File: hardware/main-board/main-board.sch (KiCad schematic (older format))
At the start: 92 parts, among them J1 BARREL_JACK, J2 CONN_01X10, J3 CONN_01X10, J4 USB_OTG, J5 CONN_02X05, J6 SMA, Q1 DDTD113ZC, Q2 DDTD113ZC, Q3 DDTD113ZC, Q4 DDTD113ZC, Q5 DDTD113ZC, Q6 FDB14N30TM, Q7 DDTD113ZC, Q8 DDTD113ZC, Q9 DDTD113ZC, SW1 SW_Push, SW2 SW_Push, SW3 SW_Push, SW4 SW_Push, U1 LD1117S33TR, U2 MAX1771, U3 STM32F302C, U4 FGPMMOPA6H, Y1 8MHz, Y2 32.768kHz

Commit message: Working on main board schematic
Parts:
- C10, C8: footprint (none) -> Capacitors_SMD:C_0805; Part (none) -> 311-1365-1-ND; Source (none) -> DigiKey
- C12: footprint (none) -> Capacitors_SMD:C_0603; Part (none) -> 311-1085-1-ND; Source (none) -> DigiKey
- C13, C17: value C -> 16p; footprint (none) -> Capacitors_SMD:C_0603; Part (none) -> 311-1751-1-ND; Source (none) -> DigiKey
- C16: footprint Capacitors_SMD:C_0603 -> Capacitors_SMD:C_0805; Part (none) -> 311-1365-1-ND
- C18: Part (none) -> 311-1085-1-ND
- C19, C20: value C -> 5p; footprint (none) -> Capacitors_SMD:C_0603; Part (none) -> 311-1054-1-ND; Source (none) -> DigiKey
- C2: footprint (none) -> Capacitors_SMD:C_0805; Part (none) -> 311-1460-1-ND; Source (none) -> DigiKey
- C4: value CP -> 150u
- C5, C6: value CP -> 3.3u; footprint (none) -> Capacitors_ThroughHole:CP_Radial_D6.3mm_P2.50mm; Part (none) -> 493-12639-1-ND; Source (none) -> DigiKey
- J5: Part (none) -> NA; Source (none) -> NA
- TP1, TP2, TP3, TP4, TP5, TP6: Part (none) -> NA; Source DigiKey -> NA
- Y1: footprint (none) -> Crystals:Crystal_SMD_HC49-SD; Part (none) -> 535-10212-1-ND; Source (none) -> DigiKey
- Y2: footprint (none) -> radio-clock:ABS07; Part (none) -> 535-9542-1-ND; Source (none) -> DigiKey
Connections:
- wire segments 360 -> 291
- no-connect marks 5 -> 6
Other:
- moved on the sheet: BT1, C8

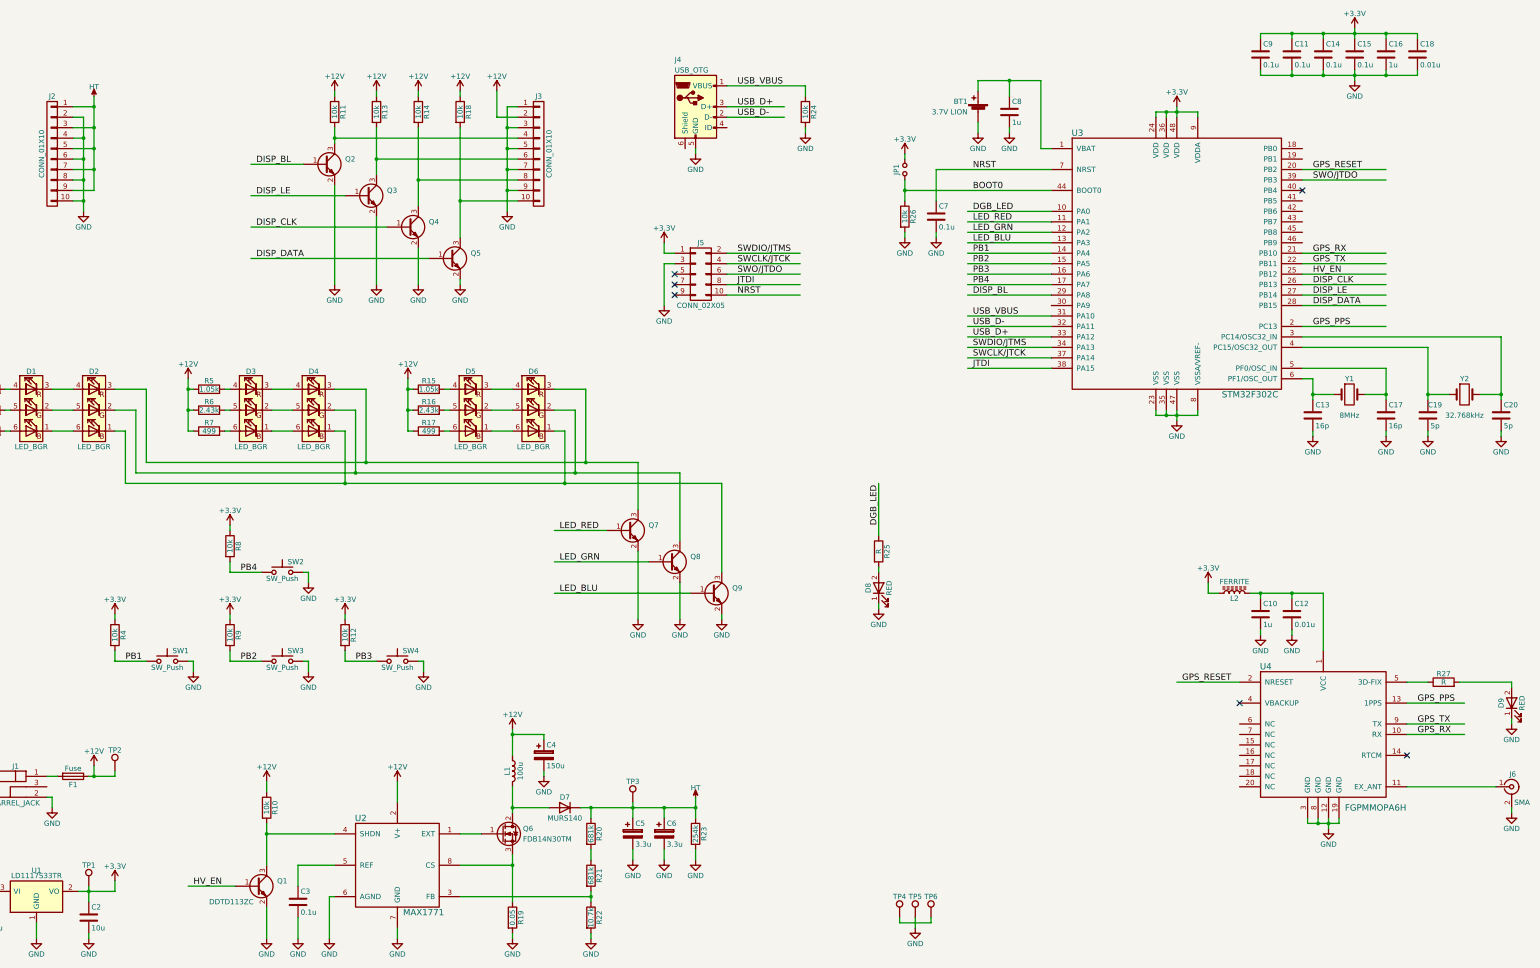
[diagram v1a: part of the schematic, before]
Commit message: Working on main board layout
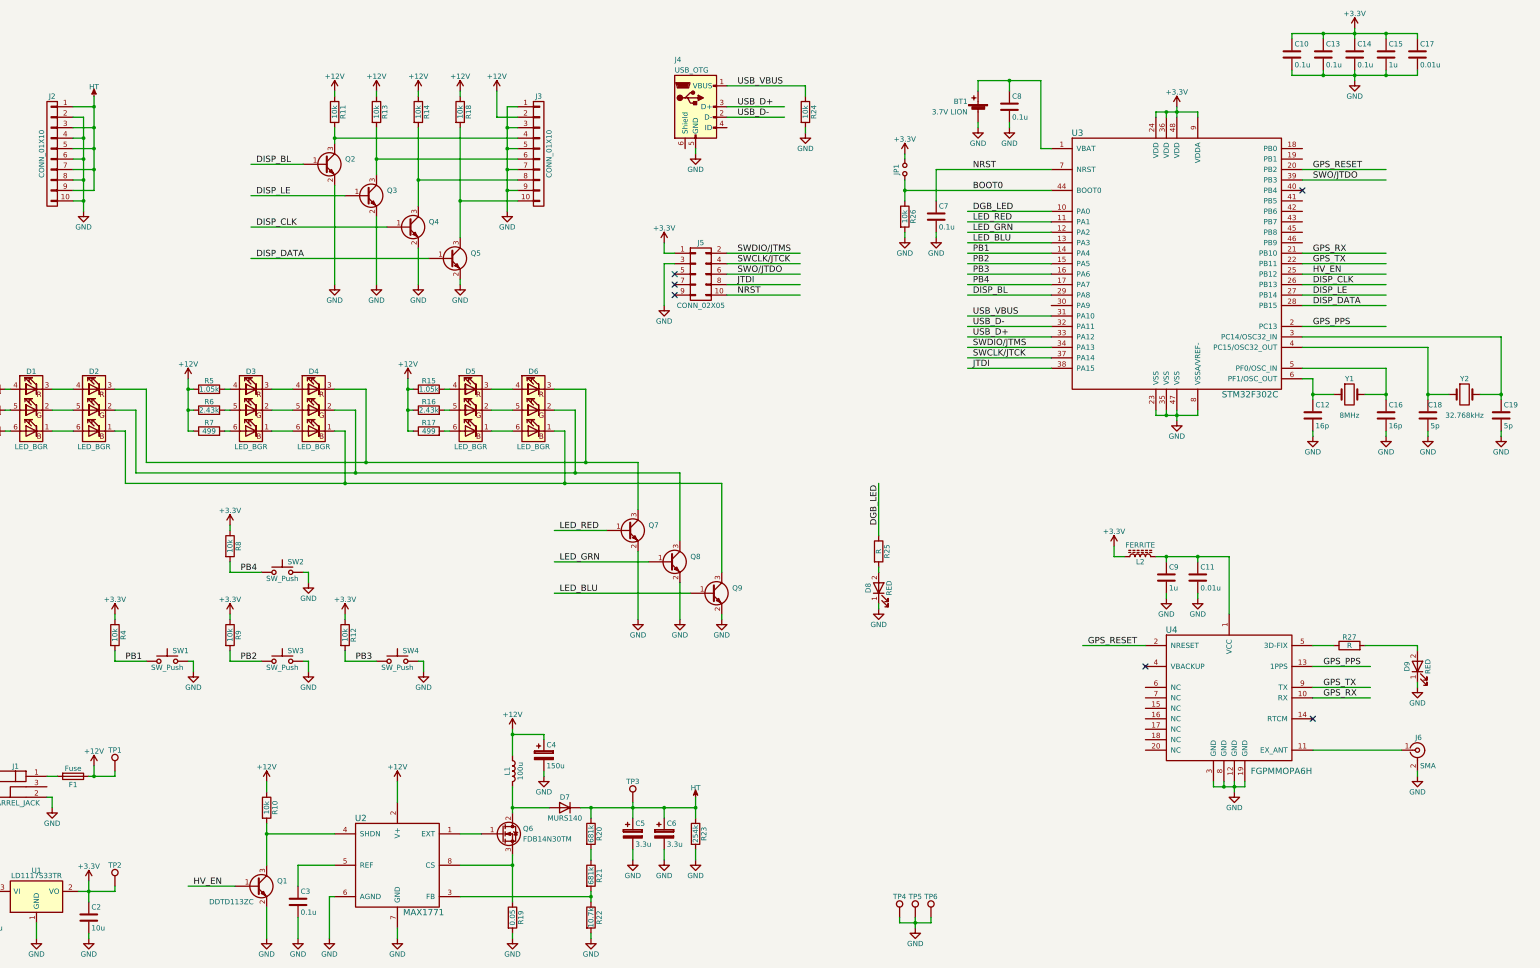
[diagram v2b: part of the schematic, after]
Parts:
- removed C8: 1u, Capacitors_SMD:C_0805, symbol C
- C4: footprint (none) -> Capacitors_ThroughHole:CP_Radial_D6.3mm_P2.50mm; Part (none) -> P15352CT-ND; Source (none) -> DigiKey
- F1: footprint (none) -> radio-clock:01110501Z; Part (none) -> F4189-ND; Source (none) -> DigiKey
- R19: footprint (none) -> Resistors_SMD:R_1206; Part (none) -> 311-.05LWCT-ND; Source (none) -> DigiKey
- R20, R21, R22, R23: footprint (none) -> Resistors_SMD:R_1206; Source (none) -> DigiKey
- renumbered C11 to C10, C12 to C11, C13 to C12, C14 to C13, C15 to C14, C16 to C15, C17 to C16, C18 to C17, C19 to C18, C20 to C19, C9 to C8, C10 to C9, TP2 to TP1, TP1 to TP2
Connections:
- wire segments 291 -> 289
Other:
- moved on the sheet: C11, C8, C9, D9, J6, L2, R27, TP2, U4

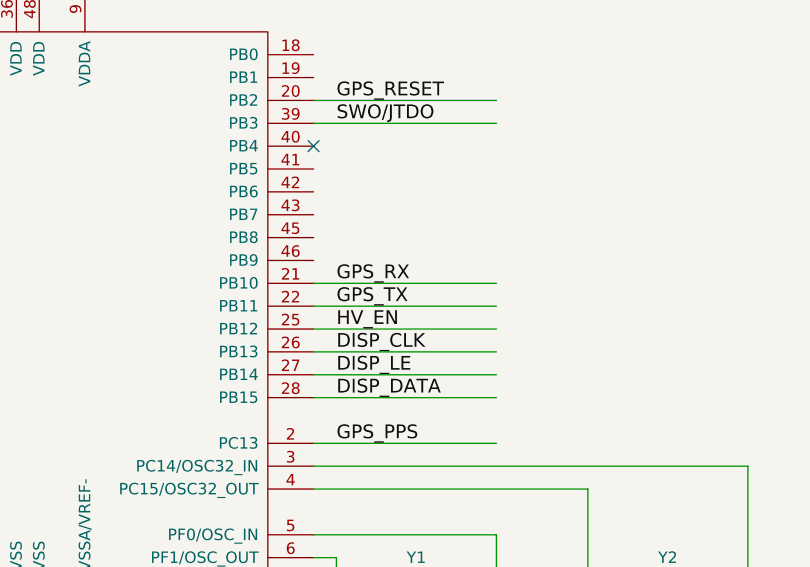
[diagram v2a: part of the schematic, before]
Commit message: Working on main board layout
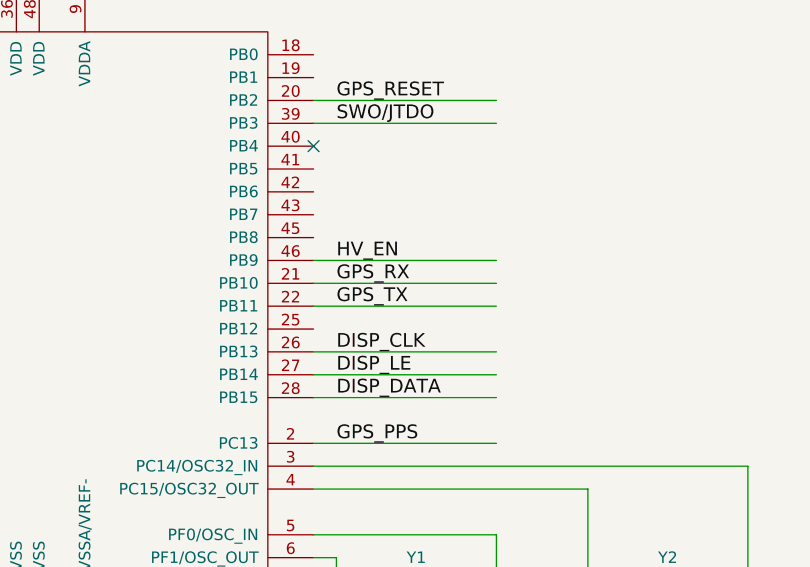
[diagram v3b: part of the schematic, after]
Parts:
- L1: footprint radio-clock:B82477R4104M100 -> radio-clock:DO3316P; Part 495-4547-1-ND -> 994-DO3316P-104MLD; Source DigiKey -> Mouser
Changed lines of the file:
@@
 F 0 "L1" V 6350 8000 50  0000 C CNN
 F 1 "100u" V 6475 8000 50  0000 C CNN
-F 2 "radio-clock:B82477R4104M100" H 6400 8000 50  0001 C CNN
+F 2 "radio-clock:DO3316P" H 6400 8000 50  0001 C CNN
 F 3 "" H 6400 8000 50  0001 C CNN
-F 4 "DigiKey" H 6400 8000 60  0001 C CNN "Source"
-F 5 "495-4547-1-ND" H 6400 8000 60  0001 C CNN "Part"
+F 4 "Mouser" H 6400 8000 60  0001 C CNN "Source"
+F 5 "994-DO3316P-104MLD" H 6400 8000 60  0001 C CNN "Part"
 	1    6400 8000
 	1    0    0    -1
@@
 Text Label 3350 9100 0    60   ~ 0
 HV_EN
-Text Label 14050 3250 0    60   ~ 0
+Text Label 14050 2950 0    60   ~ 0
 HV_EN
 $Comp
@@
 	10750 3450 11550 3450
 Wire Wire Line
-	14750 3250 13950 3250
-Wire Wire Line
 	14750 3450 13950 3450
 Wire Wire Line
@@
 	10250 9400 10250 9500
 Connection ~ 10250 9450
+Wire Wire Line
+	14750 2950 13950 2950
 $EndSCHEMATC

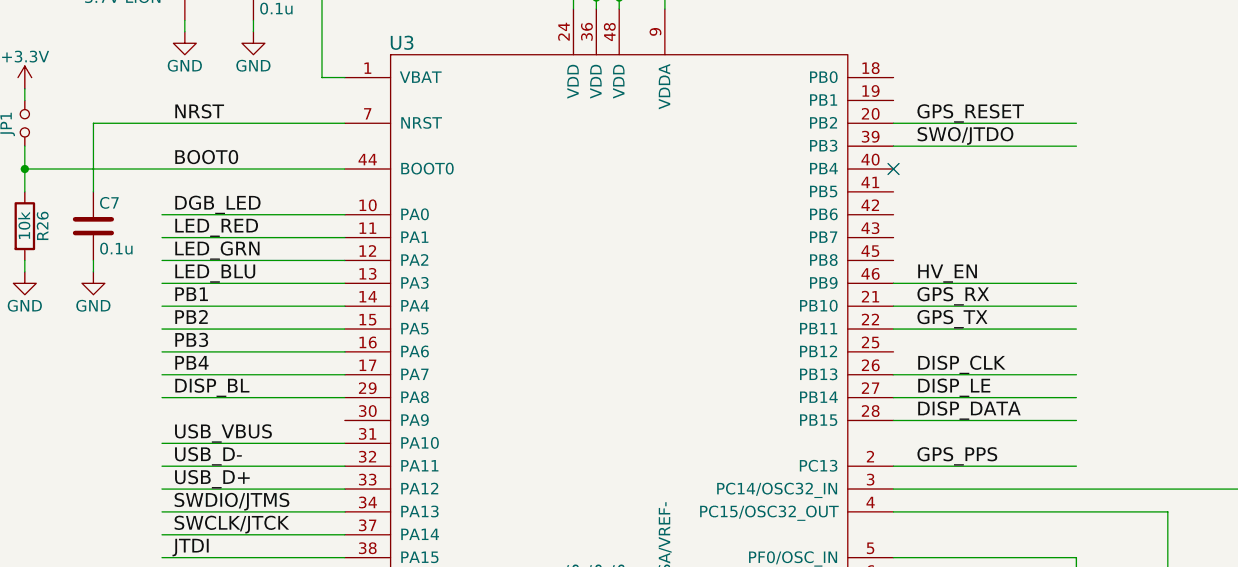
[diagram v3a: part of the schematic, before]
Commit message: Working on main board layout
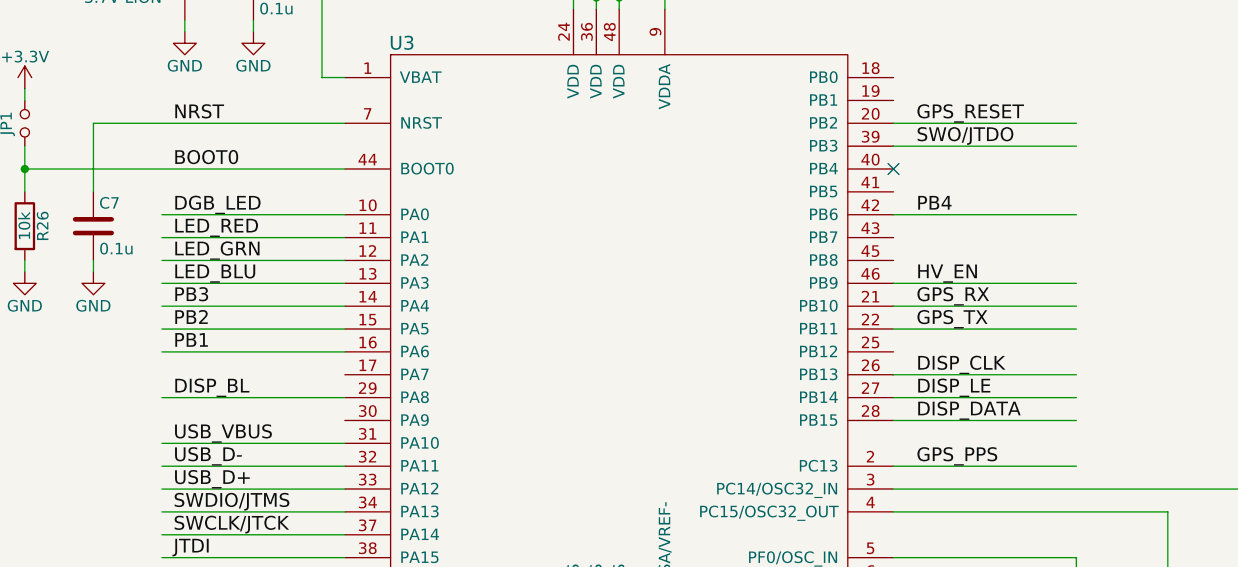
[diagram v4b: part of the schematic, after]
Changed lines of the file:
@@
 Text Label 3800 6100 0    60   ~ 0
 PB4
-Text Label 10800 3050 0    60   ~ 0
+Text Label 10800 3250 0    60   ~ 0
 PB1
 Text Label 10800 3150 0    60   ~ 0
 PB2
-Text Label 10800 3250 0    60   ~ 0
+Text Label 10800 3050 0    60   ~ 0
 PB3
-Text Label 10800 3350 0    60   ~ 0
+Text Label 14050 2650 0    60   ~ 0
 PB4
 $Comp
@@
 	11550 2450 10150 2450
 Wire Wire Line
-	10750 3350 11550 3350
-Wire Wire Line
 	10750 3250 11550 3250
 Wire Wire Line
@@
 Wire Wire Line
 	14750 2950 13950 2950
+Wire Wire Line
+	14750 2650 13950 2650
 $EndSCHEMATC

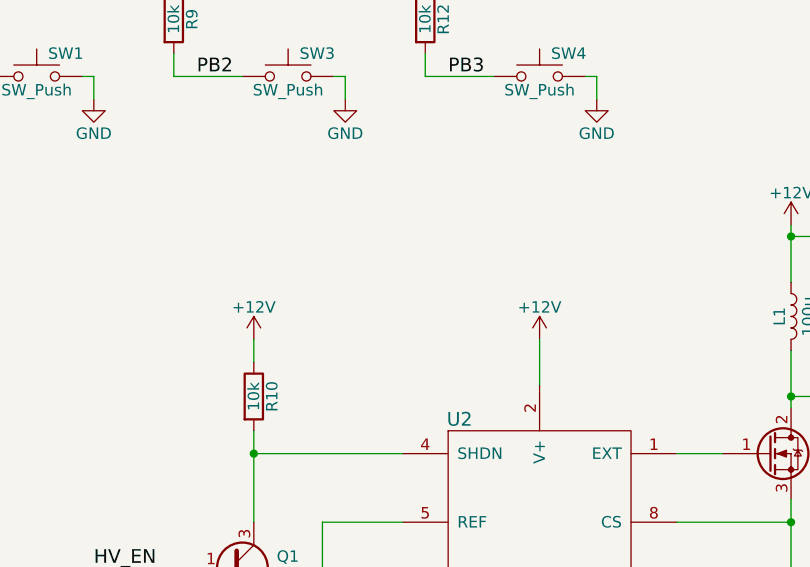
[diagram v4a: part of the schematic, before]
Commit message: Added bypass cap to MAX1771.  Cleaning up PCB design
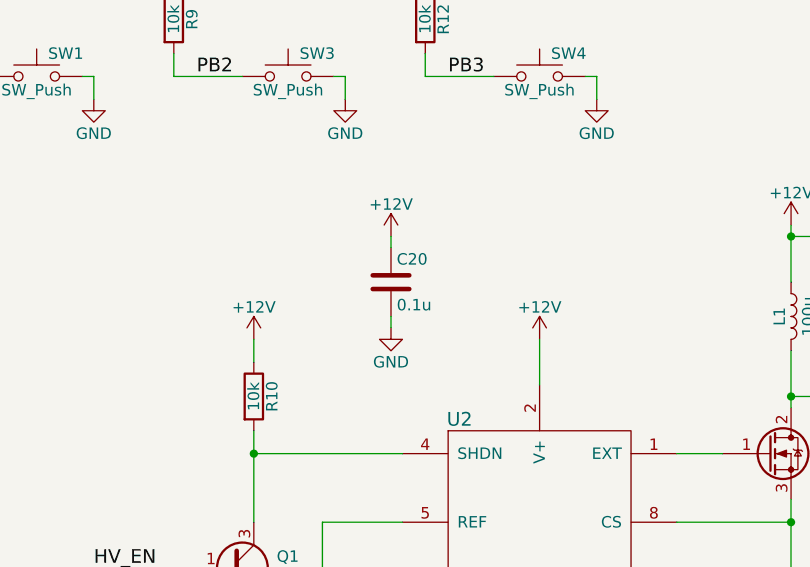
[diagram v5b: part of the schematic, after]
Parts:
- added C20: 0.1u, Capacitors_SMD:C_0603, symbol C
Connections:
- wire segments 289 -> 291

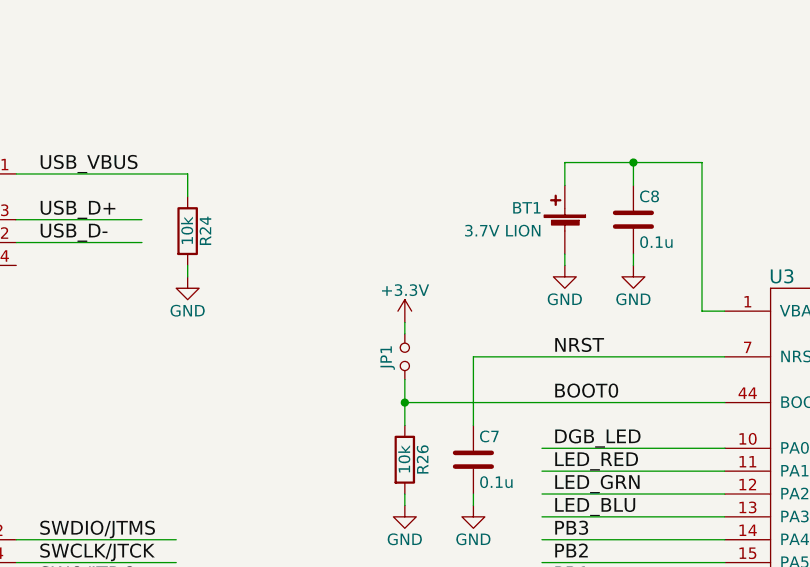
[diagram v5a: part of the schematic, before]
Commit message: Using DIP switch for BOOT mode.  Minor layout changes
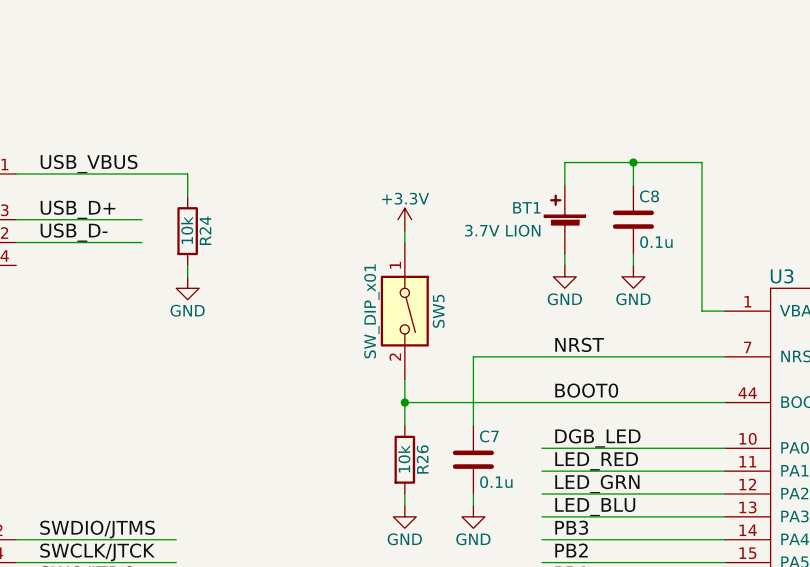
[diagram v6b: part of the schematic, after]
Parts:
- removed JP1: Jumper_NO_Small, Pin_Headers:Pin_Header_Straight_1x02_Pitch2.54mm, symbol Jumper_NO_Small
- added SW5: SW_DIP_x01, radio-clock:SDA01H1SBD, symbol SW_DIP_x01
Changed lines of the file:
@@
 SWDIO/JTMS
-$Comp
-L Jumper_NO_Small JP1
-U 1 1 58E601B3
-P 10150 2250
-F 0 "JP1" H 10150 2330 50  0000 C CNN
-F 1 "Jumper_NO_Small" H 10160 2190 50  0001 C CNN
-F 2 "Pin_Headers:Pin_Header_Straight_1x02_Pitch2.54mm" H 10150 2250 50  0001 C CNN
-F 3 "" H 10150 2250 50  0001 C CNN
-F 4 "DigiKey" H 10150 2250 60  0001 C CNN "Source"
-F 5 "3M9447-ND" H 10150 2250 60  0001 C CNN "Part"
-	1    10150 2250
-	0    -1   -1   0
-$EndComp
 $Comp
 L +3.3V #PWR55
 U 1 1 58E60AA3
-P 10150 2100
-F 0 "#PWR55" H 10150 1950 50  0001 C CNN
-F 1 "+3.3V" H 10150 2240 50  0000 C CNN
-F 2 "" H 10150 2100 50  0001 C CNN
-F 3 "" H 10150 2100 50  0001 C CNN
-	1    10150 2100
+P 10150 1700
+F 0 "#PWR55" H 10150 1550 50  0001 C CNN
+F 1 "+3.3V" H 10150 1840 50  0000 C CNN
+F 2 "" H 10150 1700 50  0001 C CNN
+F 3 "" H 10150 1700 50  0001 C CNN
+	1    10150 1700
 	1    0    0    -1
 $EndComp
@@
 	7600 5050 7600 5500
 Wire Wire Line
-	10150 2100 10150 2150
-Wire Wire Line
 	10150 2900 10150 2850
 Wire Wire Line
@@
 Wire Wire Line
 	4650 7650 4650 7700
+$Comp
+L SW_DIP_x01 SW5
+U 1 1 58F010C8
+P 10150 2050
+F 0 "SW5" H 10150 2200 50  0000 C CNN
+F 1 "SW_DIP_x01" H 10150 1900 50  0000 C CNN
+F 2 "radio-clock:SDA01H1SBD" H 10150 2050 50  0001 C CNN
+F 3 "" H 10150 2050 50  0001 C CNN
+F 4 "DigiKey" H 10150 2050 60  0001 C CNN "Source"
+F 5 "CKN10358-ND" H 10150 2050 60  0001 C CNN "Part"
+	1    10150 2050
+	0    1    1    0
+$EndComp
+Wire Wire Line
+	10150 1700 10150 1750
 $EndSCHEMATC
